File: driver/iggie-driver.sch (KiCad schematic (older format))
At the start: 38 parts, among them IC101 TSR 1-2433, IC102 STM32F405RxTx, IC103 ESP-12, J101 PSU, J102 HV, J103 DRIVE, J104 DIRECT, J105 UART, J106 ESP_FLASH, P101 SWD, X101 M3 MOUNT, X102 M3 MOUNT, X103 M3 MOUNT, X104 M3 MOUNT, X105 M3 MOUNT, X106 M3 MOUNT, X107 M3 MOUNT, X108 M3 MOUNT, Y101 26M

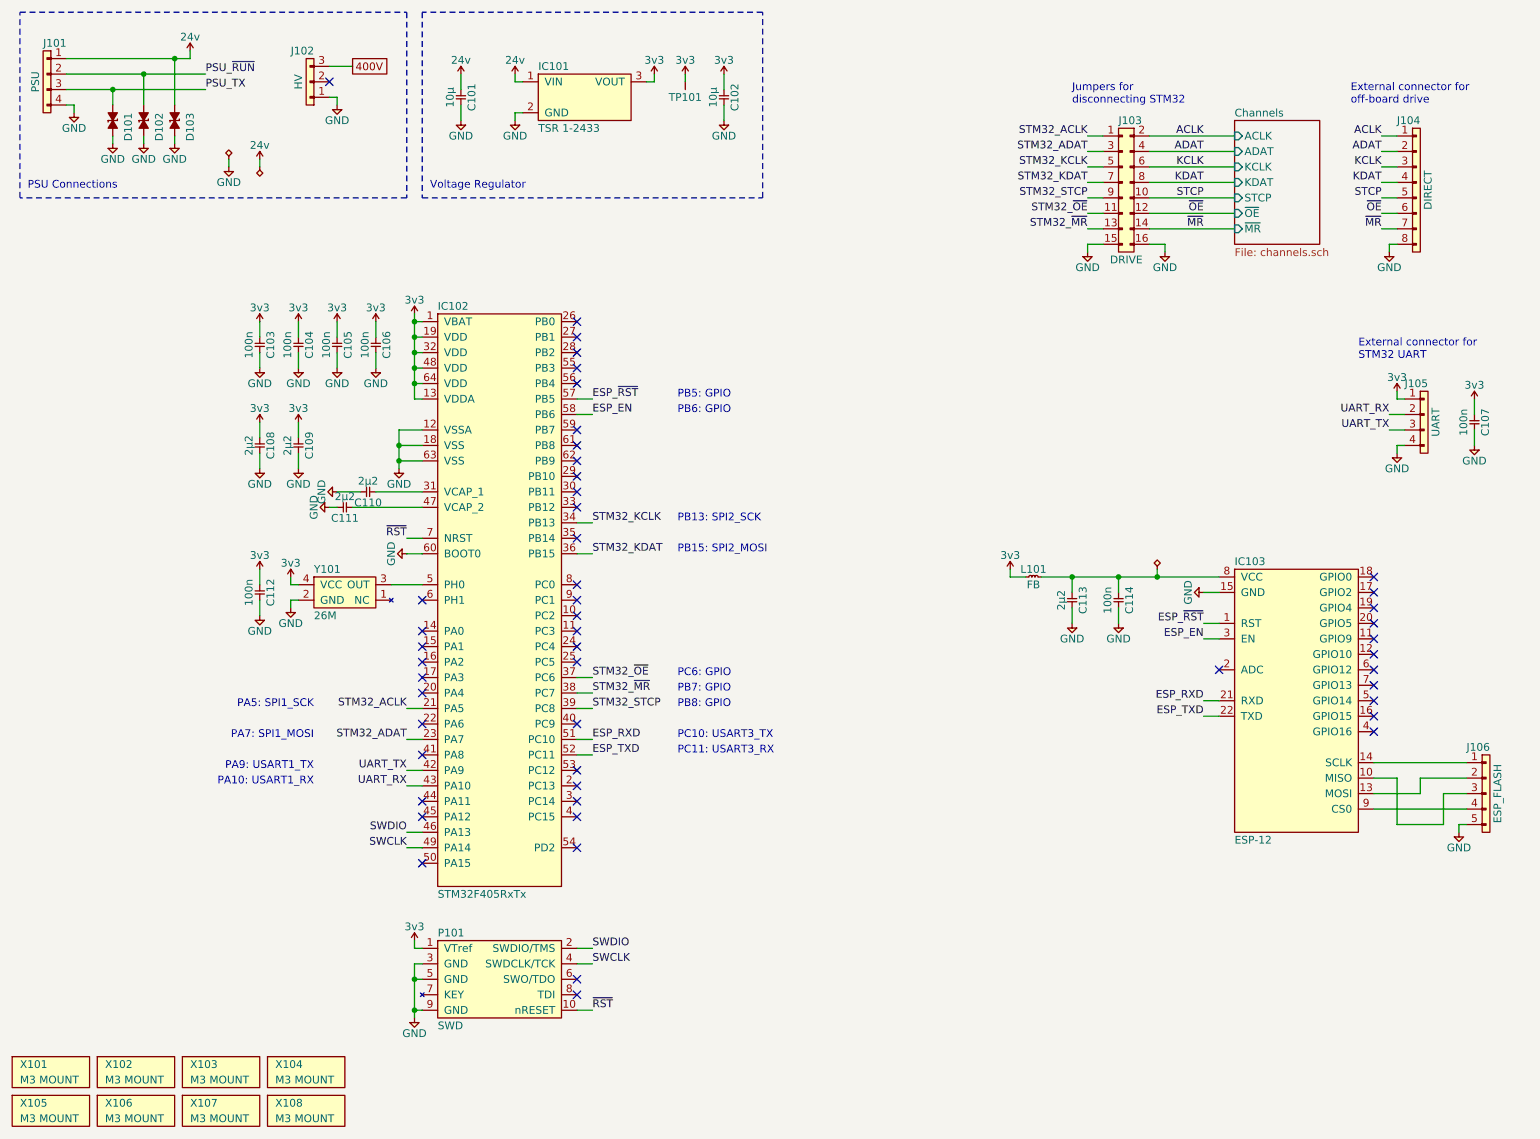
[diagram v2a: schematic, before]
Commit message: Start work on 32ch board
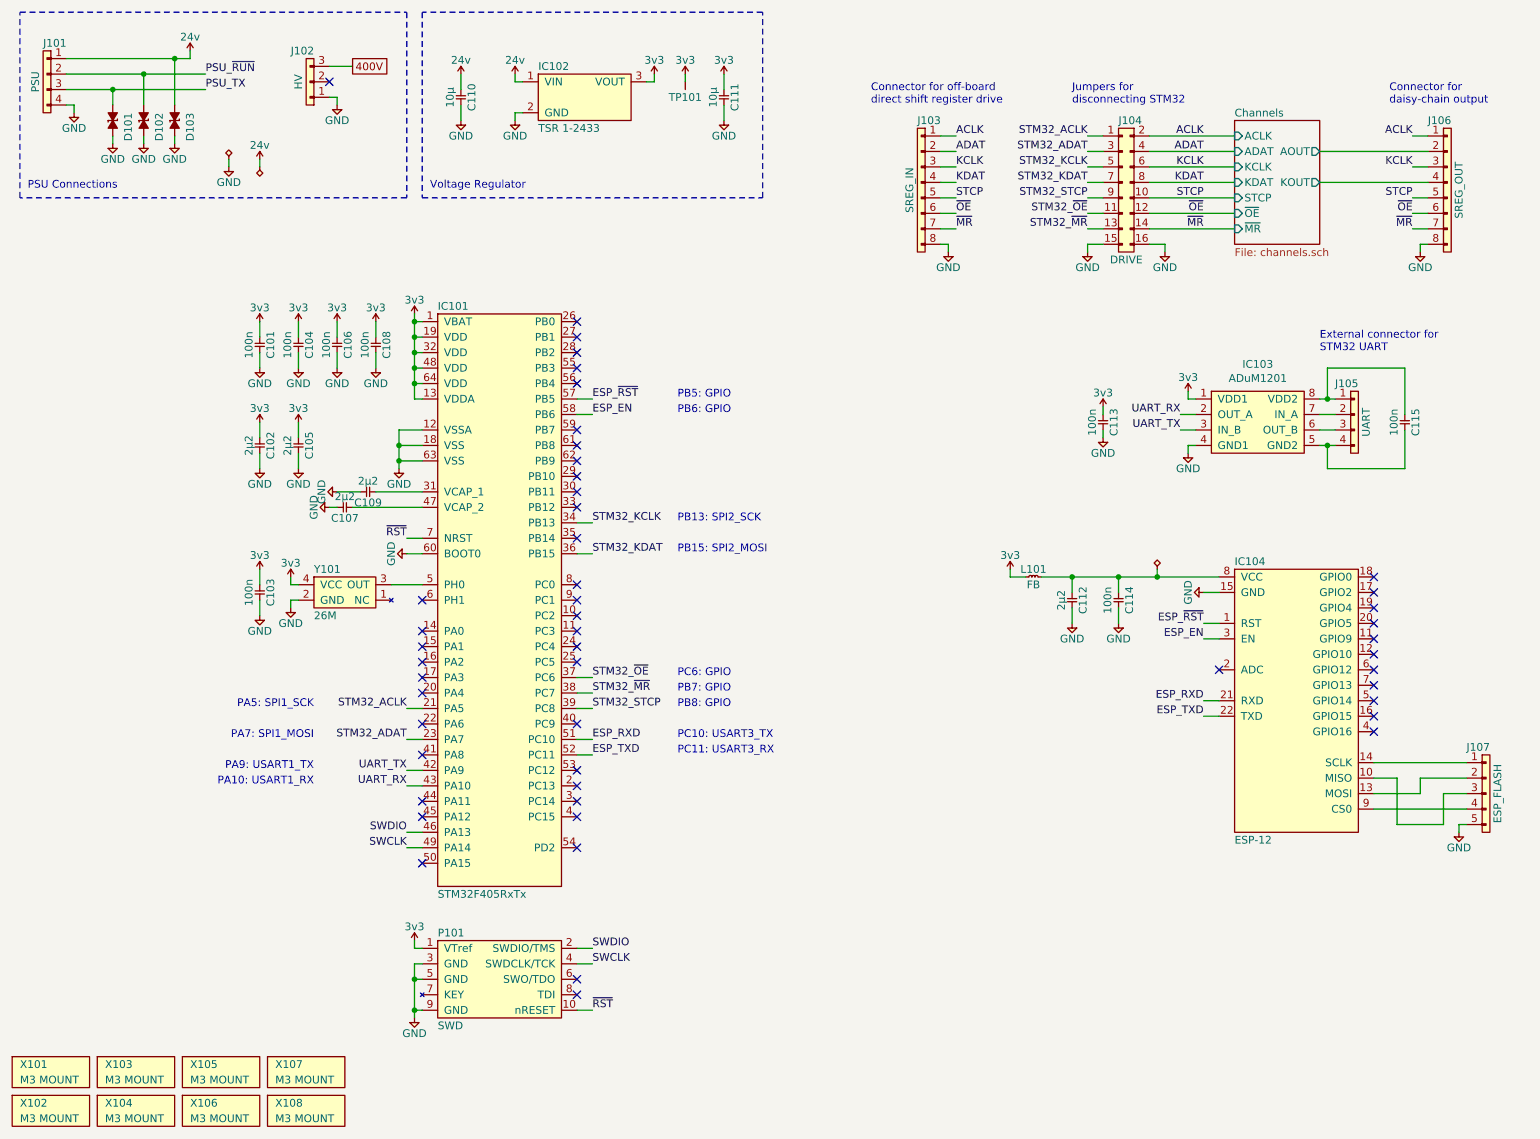
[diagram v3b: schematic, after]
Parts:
- added C113: 100n, agg:0603, symbol agg-kicad:C
- added IC103: ADuM1201, agg:SOIC-8, symbol agg-kicad:ADuM1201
- added J106: SREG_OUT, agg:MOLEX-PICOBLADE-53398-0871, symbol agg-kicad:CONN_01x08
- J103: renamed from J104; value DIRECT -> SREG_IN
- renumbered C103 to C101, C108 to C102, C112 to C103, C109 to C105, C105 to C106, C111 to C107, C106 to C108, C110 to C109, C101 to C110, C102 to C111, C113 to C112, C107 to C115, IC102 to IC101, IC101 to IC102, IC103 to IC104, J103 to J104, J106 to J107, X105 to X102, X102 to X103, X106 to X104, X103 to X105, X107 to X106, X104 to X107
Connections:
- net 3v3: now also C113.1, IC103.1 (VDD1); no longer C115.1, J105.1
- net ACLK: now also J106.1
- net GND: now also C113.2, IC103.4 (GND1), J106.8; no longer C115.2, J105.4
- net KCLK: now also J106.3
- net STCP: now also J106.5
- net UART_RX: now also IC103.2 (OUT_A); no longer J105.2
- net UART_TX: now also IC103.3 (IN_B); no longer J105.3
- net ~MR: now also J106.7
- net ~OE: now also J106.6
- new net: C115.2, IC103.5 (GND2), J105.4
- new net: IC103.6 (OUT_B), J105.3
- new net: IC103.7 (IN_A), J105.2
- new net: C115.1, IC103.8 (VDD2), J105.1
- new net Channels/AOUT: J106.2
- new net Channels/KOUT: J106.4
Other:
- note added: "Connector for off-board\ndirect shift register drive"
- note added: "Connector for\ndaisy-chain output"
- note removed: "External connector for\noff-board drive"
- moved on the sheet: C115, J103, J105

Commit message: more layout work
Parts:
- added J108: HV, agg:MOLEX-KK-254P-03, symbol agg-kicad:CONN_01x03
- added J109: PSU, agg:MOLEX-KK-254P-04, symbol agg-kicad:CONN_01x04
- IC102: value TSR 1-2433 -> TSR 1-2450; Farnell 1696319 -> 1696320
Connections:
- net 24v: now also J109.1
- net 3v3: no longer C111.1, IC102.3 (VOUT), TP101.1 (TP)
- net 400V: now also J108.3
- net GND: now also J108.1, J109.4
- new net 5v: C111.1, IC102.3 (VOUT), TP101.1 (TP)
- no-connect marks 50 -> 53
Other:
- note added: "PSU/Daisychain Connections"
- note added: "Voltage Regulators"
- note removed: "PSU Connections"
- note removed: "Voltage Regulator"
- moved on the sheet: D101, D102, D103, J101, J102
